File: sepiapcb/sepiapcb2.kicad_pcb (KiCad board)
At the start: 2 copper layers, 98.1 x 75.2 mm, 8 parts, among them SW1 SW_DPDT_x2

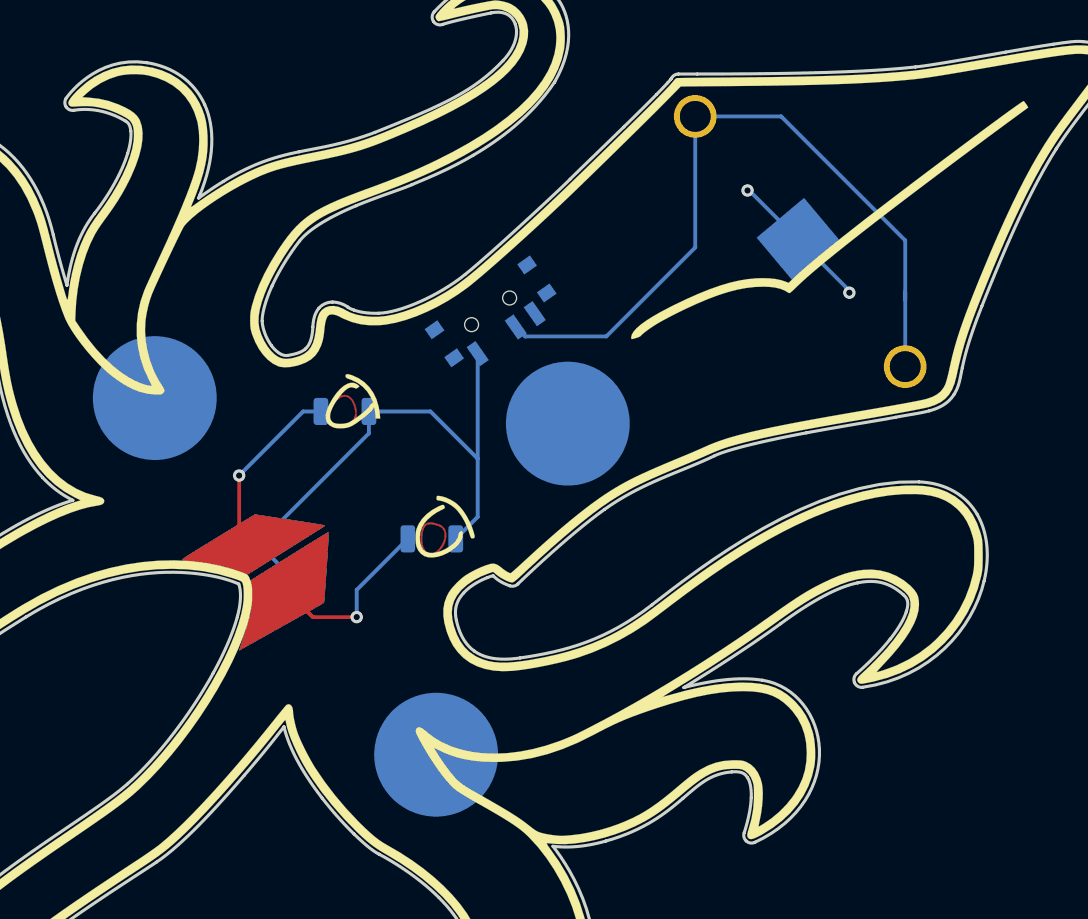
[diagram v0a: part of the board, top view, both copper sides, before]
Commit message: New battery holder footprint, logo, revision number.
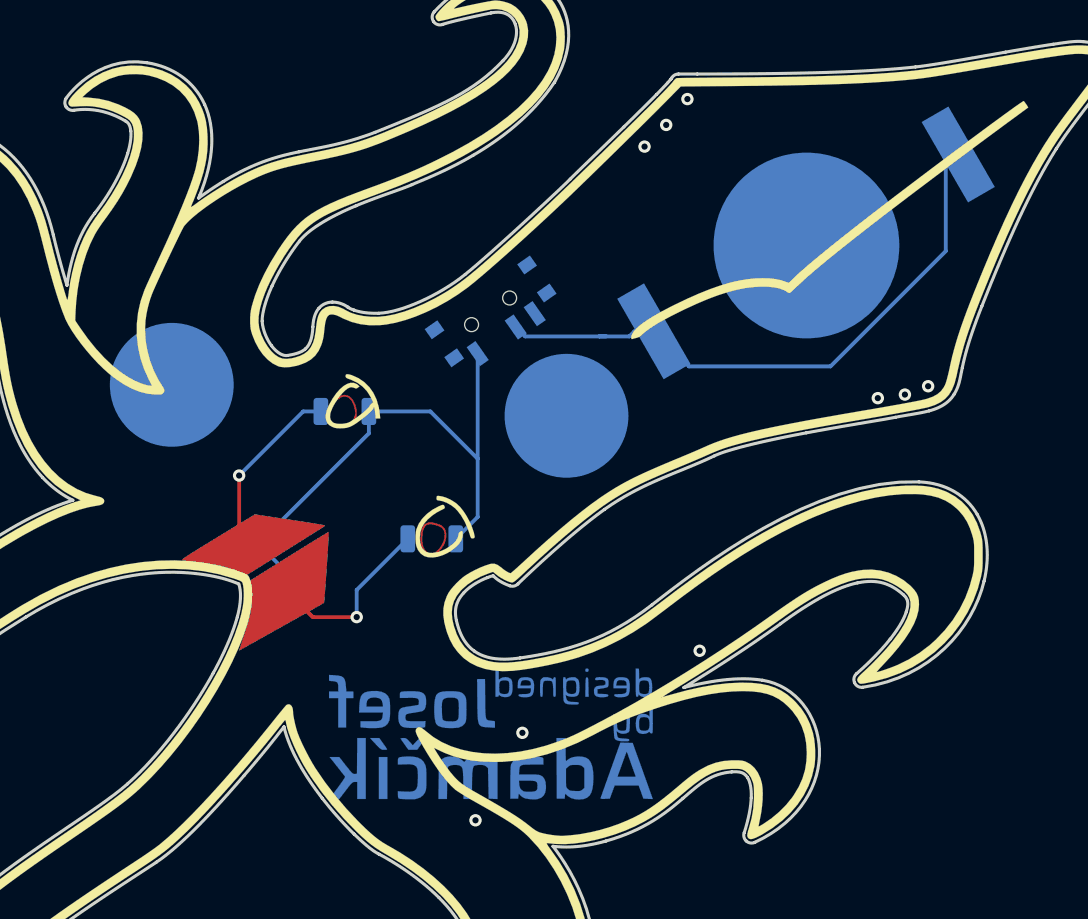
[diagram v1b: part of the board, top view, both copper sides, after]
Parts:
- removed the REF** at (62.9, 54.4)
- removed the REF** at (81.1, 77.4)
- removed the REF** at (89.6, 56.0)
- added REF**: brooch_pin_pad, sepiapcb:brooch_pin_pad, B.Cu at (64.0, 53.5)
- added REF**: brooch_pin_pad, sepiapcb:brooch_pin_pad, B.Cu at (89.5, 55.5)
- added Ref**: Val**, logos:josef_adamcik_20mm_cu_mask, B.Cu at (85.0, 80.0)
- BT1: footprint Cell_Coin_Holders:Keystone_3003_CR2032_THT -> sepiapcb:BatteryHolder_CR2032-BK-912xCR2032
- moved BT1 10.1 mm to (105.0, 44.5), turned to 30 degrees
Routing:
- net +3V0: track 48.2 -> 39.2 mm
- net GND: track 32.9 -> 28.1 mm, vias 4 -> 11
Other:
- board text added: "SepaBadge rev 2"

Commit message: wip
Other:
- board text added: "SepiaBadge rev 2"
- board text removed: "SepaBadge rev 2"
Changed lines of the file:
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@@
   (page A4)
   (layers
-    (0 F.Cu signal)
+    (0 F.Cu signal hide)
     (31 B.Cu signal)
-    (32 B.Adhes user)
-    (33 F.Adhes user)
+    (32 B.Adhes user hide)
+    (33 F.Adhes user hide)
     (34 B.Paste user)
-    (35 F.Paste user)
+    (35 F.Paste user hide)
     (36 B.SilkS user)
-    (37 F.SilkS user)
+    (37 F.SilkS user hide)
     (38 B.Mask user)
-    (39 F.Mask user)
-    (40 Dwgs.User user)
-    (41 Cmts.User user)
-    (42 Eco1.User user)
-    (43 Eco2.User user)
+    (39 F.Mask user hide)
+    (40 Dwgs.User user hide)
+    (41 Cmts.User user hide)
+    (42 Eco1.User user hide)
+    (43 Eco2.User user hide)
     (44 Edge.Cuts user)
-    (45 Margin user)
+    (45 Margin user hide)
     (46 B.CrtYd user)
-    (47 F.CrtYd user)
+    (47 F.CrtYd user hide)
     (48 B.Fab user)
-    (49 F.Fab user)
+    (49 F.Fab user hide)
   )
   (setup
@@
     (mod_text_width 0.15)
     (pad_size 1.524 1.524)
-    (pad_drill 0.762)
+    (pad_drill 1.1)
     (pad_to_mask_clearance 0.051)
     (solder_mask_min_width 0.25)
@@
     )
   )
-  (gr_text "SepaBadge\nrev 2" (at 64.84 45.85) (layer B.SilkS)
+  (gr_text "SepiaBadge\nrev 2" (at 65.4 45.09 20) (layer B.SilkS)
     (effects (font (size 1.5 1.5) (thickness 0.3)) (justify mirror))
   )
